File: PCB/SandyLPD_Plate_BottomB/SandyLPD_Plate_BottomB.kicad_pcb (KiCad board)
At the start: 2 copper layers, 124.4 x 83 mm, 9 parts

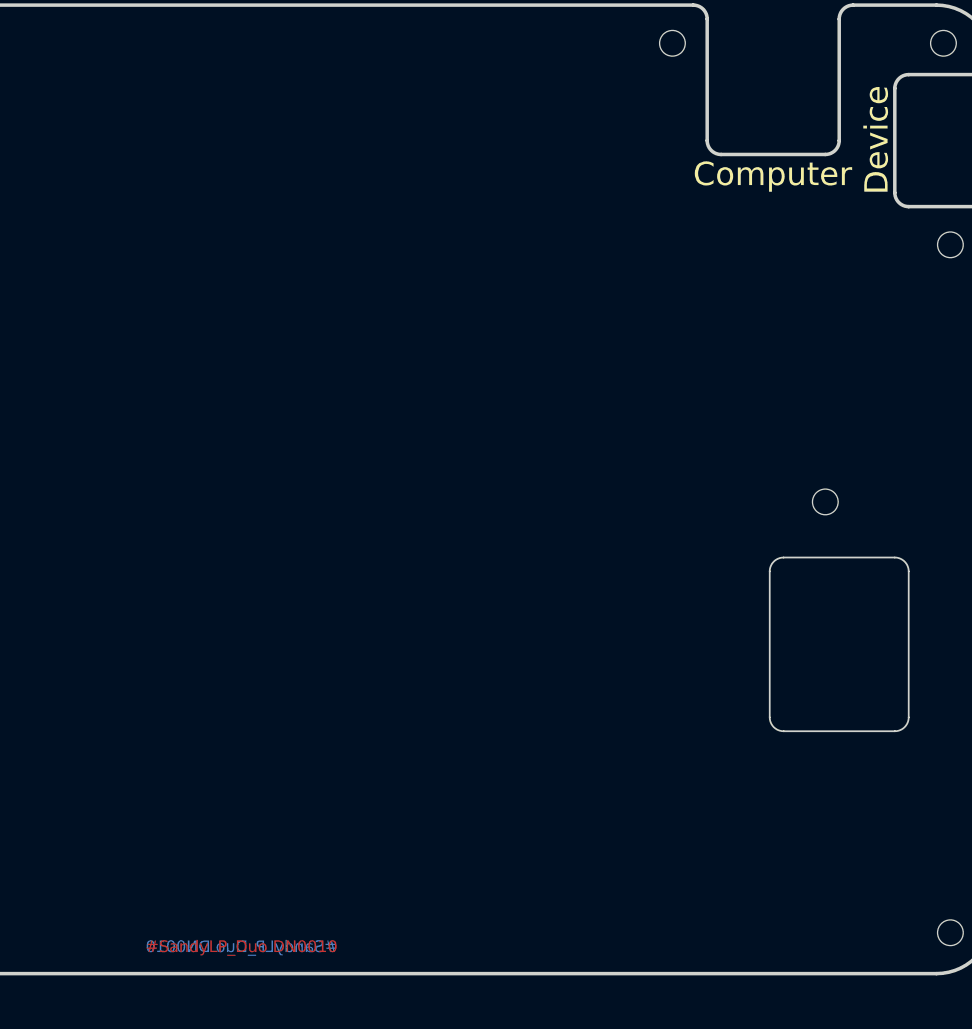
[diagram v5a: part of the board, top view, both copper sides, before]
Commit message: シルク追加
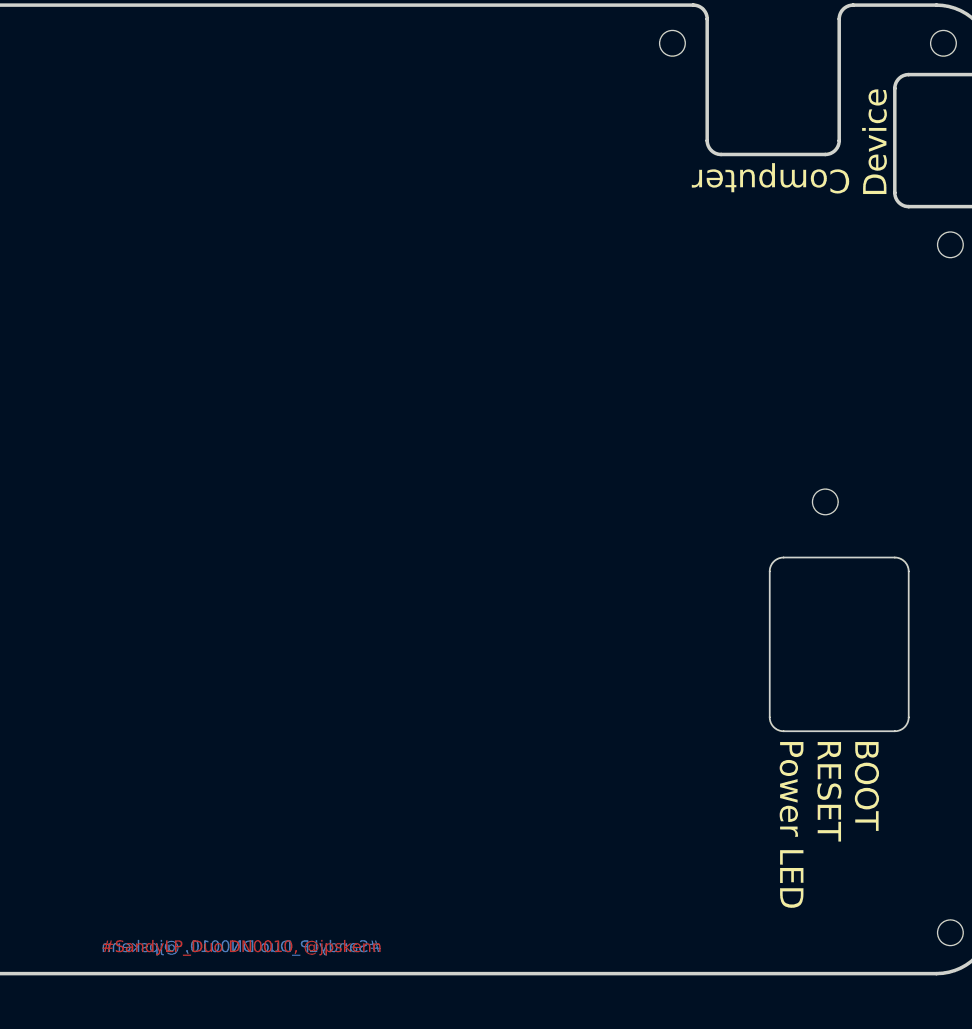
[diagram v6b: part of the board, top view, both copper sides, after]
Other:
- board text added: "#SandyLP_Duo DN0010, @jpskenn"
- board text added: "BOOT RESET Power LED"
- board text added: "Power LED RESET BOOT"
- board text removed: "#SandyLP_Duo DN0010"
- board text removed: "⌨️"

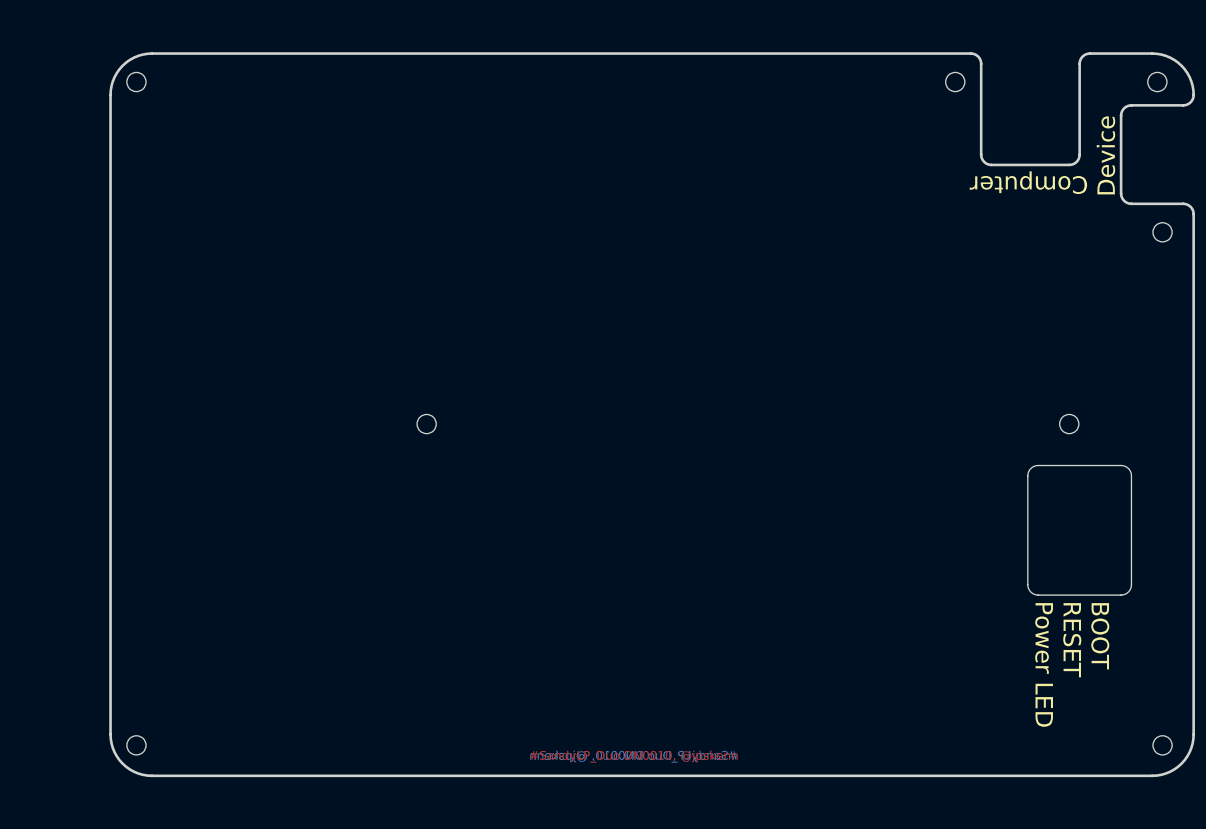
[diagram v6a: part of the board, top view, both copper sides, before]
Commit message: ボトムプレートの外形を、基板Baseと同形状に戻す。
仕様では左右端を斜めにして、テント時の小指側持ち上がりを防止する予定だった。
しかし、ケースなどを考慮すると、ボトムの外形が異なると不都合なため、基板Baseと同形状とする。
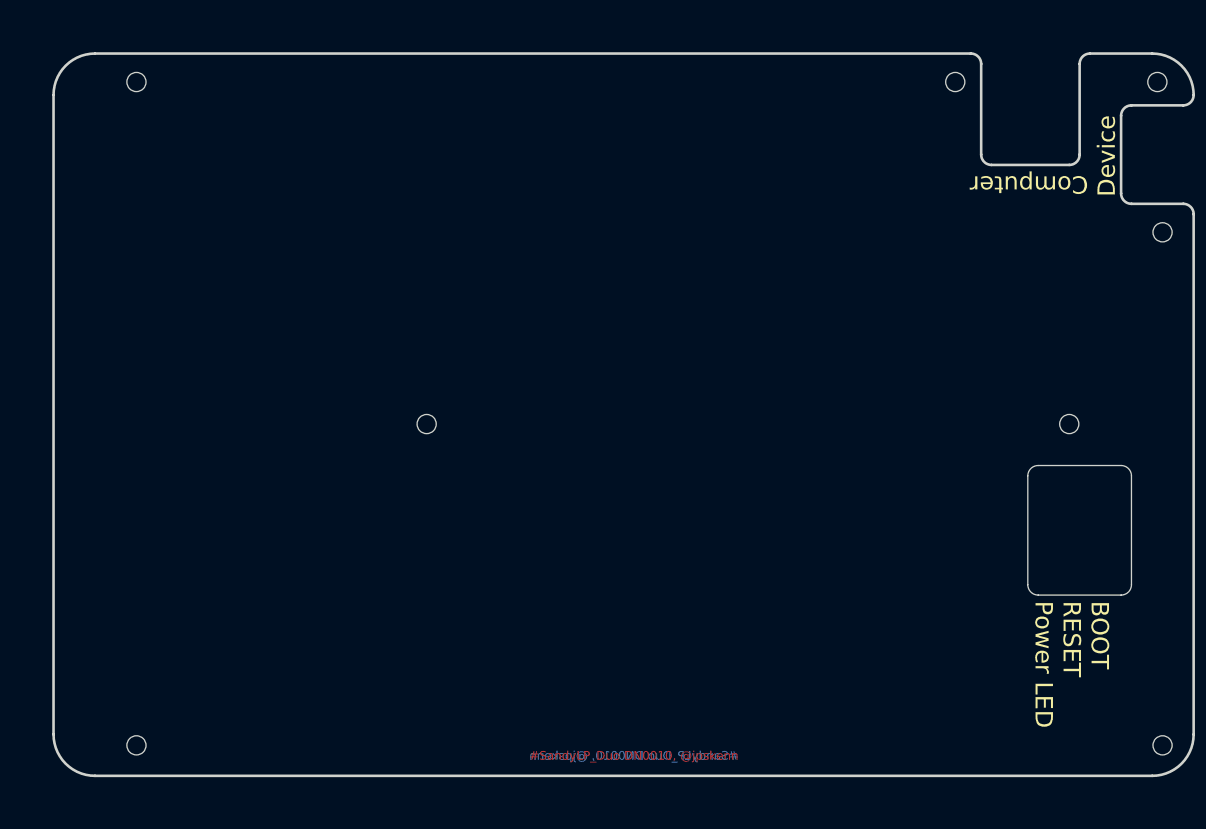
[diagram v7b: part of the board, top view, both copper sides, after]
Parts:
- REF**: footprint locallib:SandyLP-Duo_outline_BottomB_narrow_edge -> locallib:SandyLP-Duo_outline_BottomB
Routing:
- added copper zone on B.Cu, net (none)
- added copper zone on F.Cu, net (none)
- removed copper zone on B.Cu, net GND
- removed copper zone on F.Cu, net GND
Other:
- board size 124.4 x 83 mm -> 131 x 83 mm
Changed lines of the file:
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@@
 	)
 	(net 0 "")
-	(net 1 "GND")
 	(footprint "locallib:MountingHole_2.2mm_M2_no_REF"
 		(layer "F.Cu")
@@
 			)
 		)
-		(property "Description" ""
+		(property "Description" "Mounting Hole without connection"
 			(at 0 0 0)
 			(unlocked yes)
@@
 			)
 		)
-		(property ki_fp_filters "MountingHole*Pad*")
+		(property ki_fp_filters "MountingHole*")
 		(sheetname "ルート")
 		(sheetfile "SandyLPD_Plate_BottomB.kicad_sch")
-		(attr exclude_from_pos_files)
+		(attr exclude_from_pos_files exclude_from_bom)
 		(fp_circle
 			(center 0 0)
@@
 			)
 		)
-		(property "Description" ""
+		(property "Description" "Mounting Hole without connection"
 			(at 0 0 180)
 			(unlocked yes)
@@
 			)
 		)
-		(property ki_fp_filters "MountingHole*Pad*")
+		(property ki_fp_filters "MountingHole*")
 		(sheetname "ルート")
 		(sheetfile "SandyLPD_Plate_BottomB.kicad_sch")
-		(attr exclude_from_pos_files)
+		(attr exclude_from_pos_files exclude_from_bom)
 		(fp_circle
 			(center 0 0)
@@
 			)
 		)
-		(property "Description" ""
+		(property "Description" "Mounting Hole without connection"
 			(at 0 0 0)
 			(unlocked yes)
@@
 			)
 		)
-		(property ki_fp_filters "MountingHole*Pad*")
+		(property ki_fp_filters "MountingHole*")
 		(sheetname "ルート")
 		(sheetfile "SandyLPD_Plate_BottomB.kicad_sch")
-		(attr exclude_from_pos_files)
+		(attr exclude_from_pos_files exclude_from_bom)
 		(fp_circle
 			(center 0 0)
@@
 		)
 	)
-	(footprint "locallib:SandyLP-Duo_outline_BottomB_narrow_edge"
+	(footprint "locallib:SandyLP-Duo_outline_BottomB"
 		(locked yes)
 		(layer "F.Cu")
@@
 			)
 		)
-		(property "Footprint" "locallib:SandyLP-Duo_outline_BottomB_narrow_edge"
+		(property "Footprint" "locallib:SandyLP-Duo_outline_BottomB"
 			(at 0 0 0)
 			(layer "F.Fab")
@@
 			)
 		)
-		(attr through_hole)
+		(attr through_hole board_only)
 		(fp_line
 			(start -140.49375 -66.675)
@@
 		)
 		(fp_line
-			(start -129.182921 33.337528)
-			(end -129.182921 -66.674972)
-			(stroke
-				(width 0.15)
-				(type solid)
-			)
-			(layer "Dwgs.User")
-		)
-		(fp_line
 			(start -121.94375 -50.70629)
 			(end -121.94375 -47.55629)
@@
 		)
 		(fp_line
-			(start -129.182921 26.123471)
-			(end -129.182921 -47.32504)
+			(start -135.731364 26.123471)
+			(end -135.731364 -47.32504)
 			(stroke
 				(width 0.3)
@@
 		(fp_line
 			(start -30.360962 -52.08754)
-			(end -124.420421 -52.08754)
+			(end -130.968864 -52.08754)
 			(stroke
 				(width 0.3)
@@
 		(fp_line
 			(start -9.525004 30.885971)
-			(end -124.420421 30.885971)
+			(end -130.968864 30.885971)
 			(stroke
 				(width 0.3)
@@
 		)
 		(fp_arc
-			(start -129.182921 -47.32504)
-			(mid -127.788017 -50.692636)
-			(end -124.420421 -52.08754)
+			(start -135.731364 -47.32504)
+			(mid -134.33646 -50.692636)
+			(end -130.968864 -52.08754)
 			(stroke
 				(width 0.3)
@@
 		)
 		(fp_arc
-			(start -124.420421 30.885971)
-			(mid -127.788017 29.491067)
-			(end -129.182921 26.123471)
+			(start -130.968864 30.885971)
+			(mid -134.33646 29.491067)
+			(end -135.731364 26.123471)
 			(stroke
 				(width 0.3)
@@
 		)
 		(group ""
-			(members "08d7137f-7bb0-441a-8919-cfae6b3c3d0a" "37115a94-a1b5-4d89-a13c-1938b68ecf9d"
-				"3b8b85a1-c0cf-42fc-9018-b653c67bc99e" "44e9428c-2661-4ba1-b625-965da7066172"
-				"4987b5f4-7098-4bb2-8a6d-87f0f99c8ad0" "a17ef407-88aa-4c6e-85ba-e07cf4159ff2"
-				"bd28584d-091f-4e2e-9219-60f63d9db290"
+			(members "1d8cc2c4-e88a-4503-85c8-7cdc7f5fe951" "2545b97a-3b06-4e62-a889-0e7fa287b5b0"
+				"335916c3-252b-42c0-9c90-4ce8791a3f72" "4f729eca-73d5-4b9c-949f-91c84362a6af"
+				"54e35339-30db-4bf0-be88-1a860aa4a867" "8231154a-c87d-478c-8707-29be634ed9fb"
+				"a075de65-9eec-40e8-a3e7-cc5b94b3eb27"
 			)
 		)
@@
 			)
 		)
-		(property "Description" ""
+		(property "Description" "Mounting Hole without connection"
 			(at 0 0 0)
 			(unlocked yes)
@@
 			)
 		)
-		(property ki_fp_filters "MountingHole*Pad*")
+		(property ki_fp_filters "MountingHole*")
 		(sheetname "ルート")
 		(sheetfile "SandyLPD_Plate_BottomB.kicad_sch")
-		(attr exclude_from_pos_files)
+		(attr exclude_from_pos_files exclude_from_bom)
 		(fp_circle
 			(center 0 0)
@@
 			)
 		)
-		(property "Description" ""
+		(property "Description" "Mounting Hole without connection"
 			(at 0 0 0)
 			(unlocked yes)
@@
 			)
 		)
-		(property ki_fp_filters "MountingHole*Pad*")
+		(property ki_fp_filters "MountingHole*")
 		(sheetname "ルート")
 		(sheetfile "SandyLPD_Plate_BottomB.kicad_sch")
-		(attr exclude_from_pos_files)
+		(attr exclude_from_pos_files exclude_from_bom)
 		(fp_circle
 			(center 0 0)
@@
 	(gr_text_box "DIP Switch\n  1. Power LED ON/OFF\n\n  2.\n\n  3.\n\n  4."
 		(start 92.928734 74.528405)
-		(end 143.475636 104.103429)
+		(end 133.950636 104.103429)
 		(layer "F.SilkS")
 		(effects
@@
 		)
 		(render_cache "DIP Switch\n  1. Power LED ON/OFF\n\n  2.\n\n  3.\n\n  4."
-			-0
+			0
 			(polygon
 				(pts
@@
 	)
 	(zone
-		(net 1)
-		(net_name "GND")
+		(net 0)
+		(net_name "")
 		(layers "F&B.Cu")
 		(hatch edge 0.508)

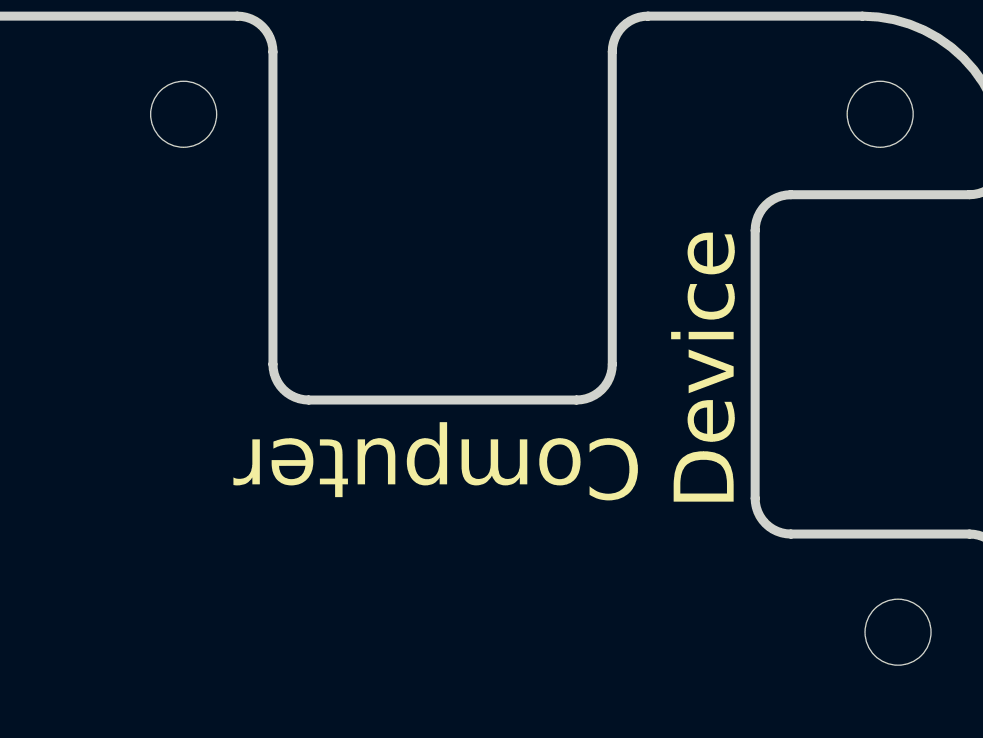
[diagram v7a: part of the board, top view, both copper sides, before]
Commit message: USBコネクタのアイコン表記 #30
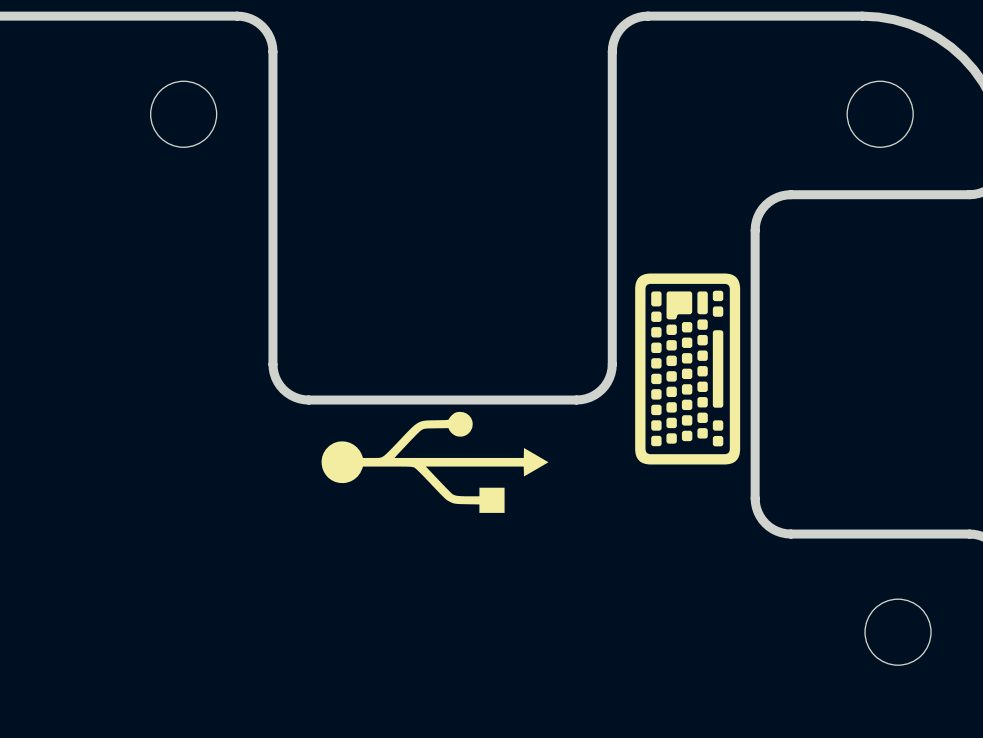
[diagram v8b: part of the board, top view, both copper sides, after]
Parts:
- added G***: LOGO, locallib:ICON_USB, F.Cu at (135.4, 46.9)
- added G***: LOGO, locallib:ICON_USB, B.Cu at (135.8, 46.9)
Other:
- board text added: "⌨️"
- board text removed: "Computer"
- board text removed: "Device"
